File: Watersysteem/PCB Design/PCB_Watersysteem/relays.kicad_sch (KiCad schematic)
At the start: 21 parts, among them J14 Pomp1, J15 Pomp2, J16 Pomp3, J17 Pomp4, K1 AHQSS105DM2FA0G, K2 AHQSS105DM2FA0G, K3 AHQSS105DM2FA0G, K4 AHQSS105DM2FA0G, K5 AHQSS105DM2FA0G, K6 AHQSS105DM2FA0G, K7 AHQSS105DM2FA0G, Q1 PN2222A

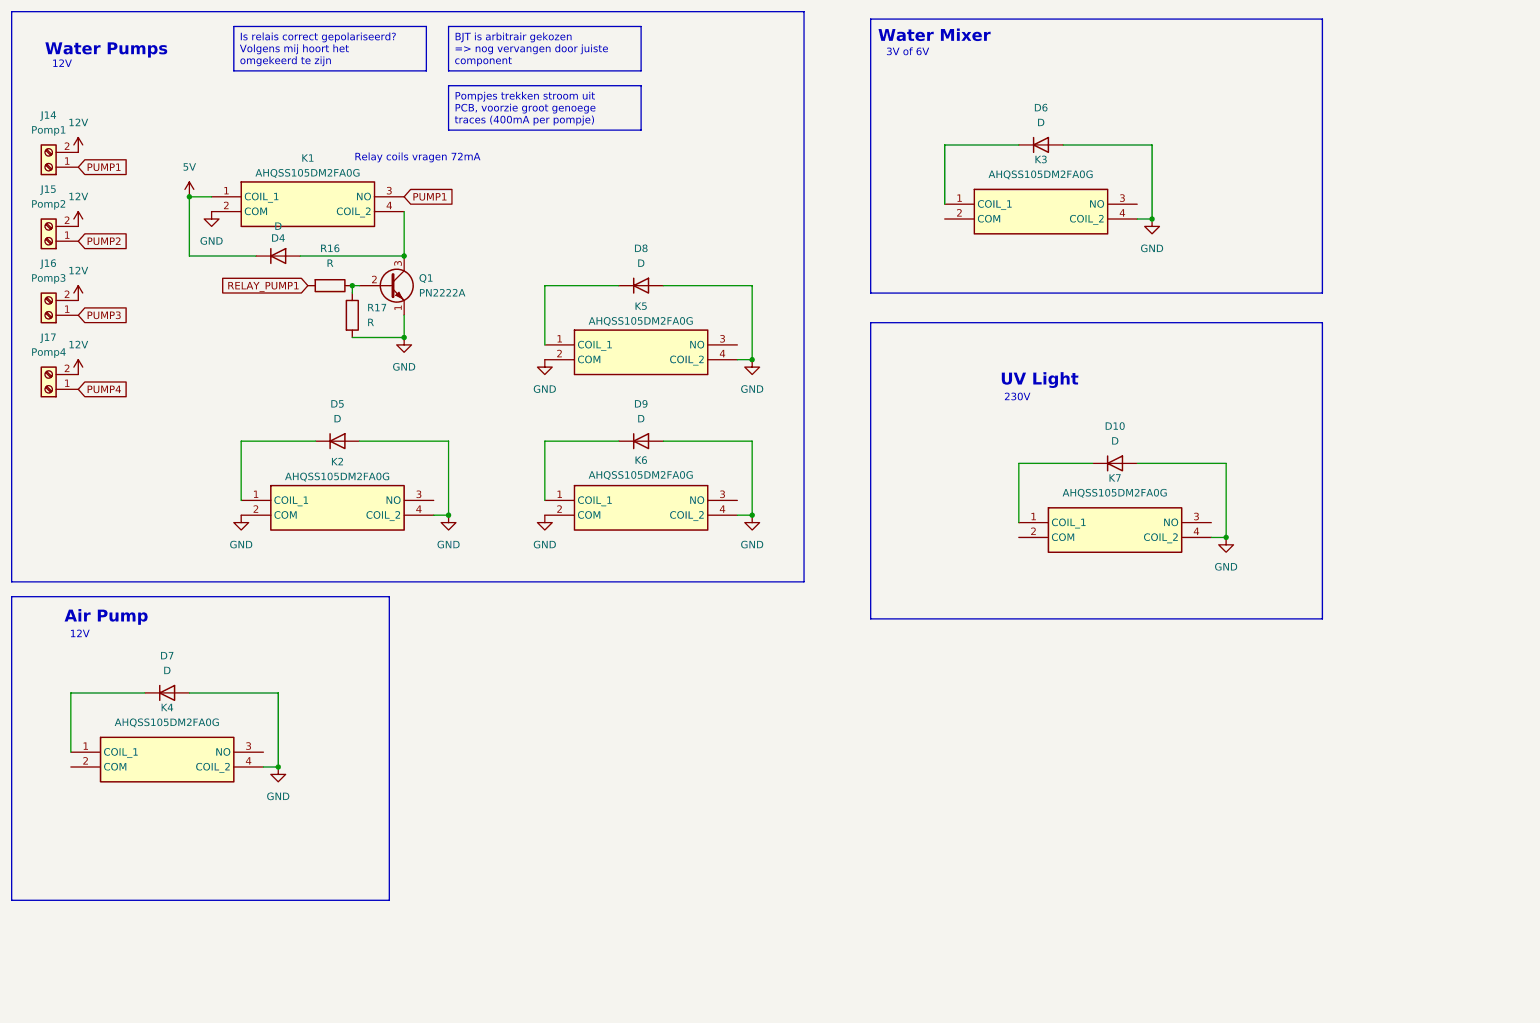
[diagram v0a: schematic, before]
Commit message: Update PCB
Extra terminals
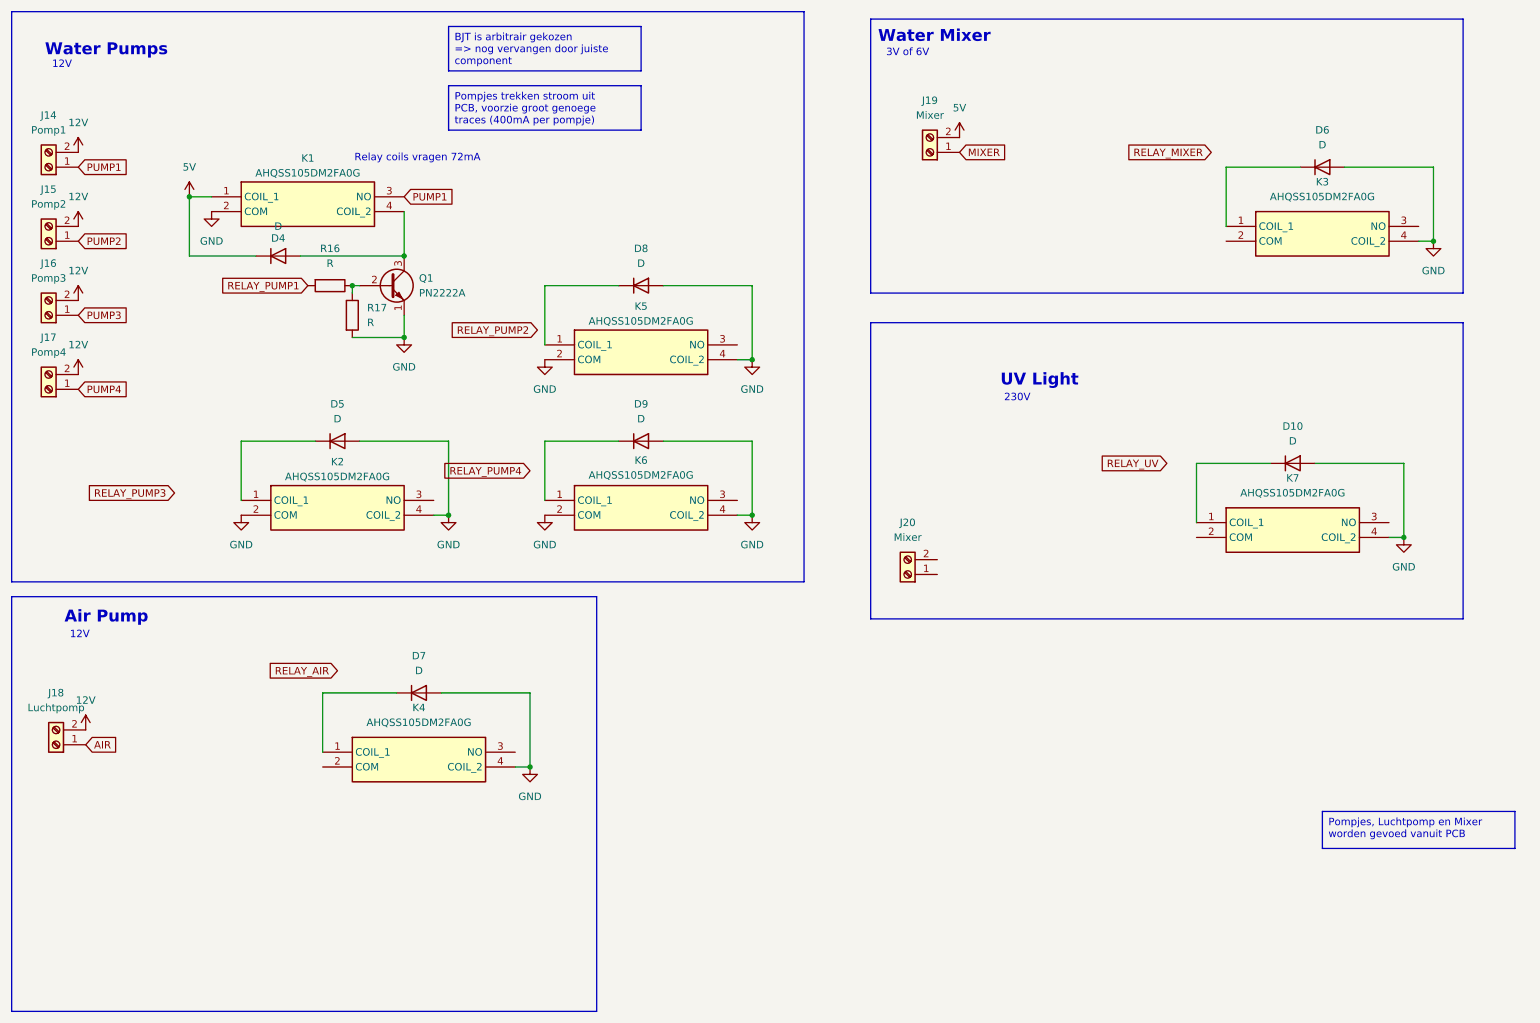
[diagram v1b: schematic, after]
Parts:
- added J18: Luchtpomp, symbol Connector:Screw_Terminal_01x02
- added J19, J20: Mixer, symbol Connector:Screw_Terminal_01x02
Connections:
- net 12V: now also J18.2 (Pin_2)
- net 5V: now also J19.2 (Pin_2)
- new net AIR: J18.1 (Pin_1)
- new net MIXER: J19.1 (Pin_1)
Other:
- moved on the sheet: D10, D6, D7, K3, K4, K7

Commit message: Update PCB
relaisschakelingen verder afgewerkt, endstops afgewerkt, bezig met ultrasone sensors
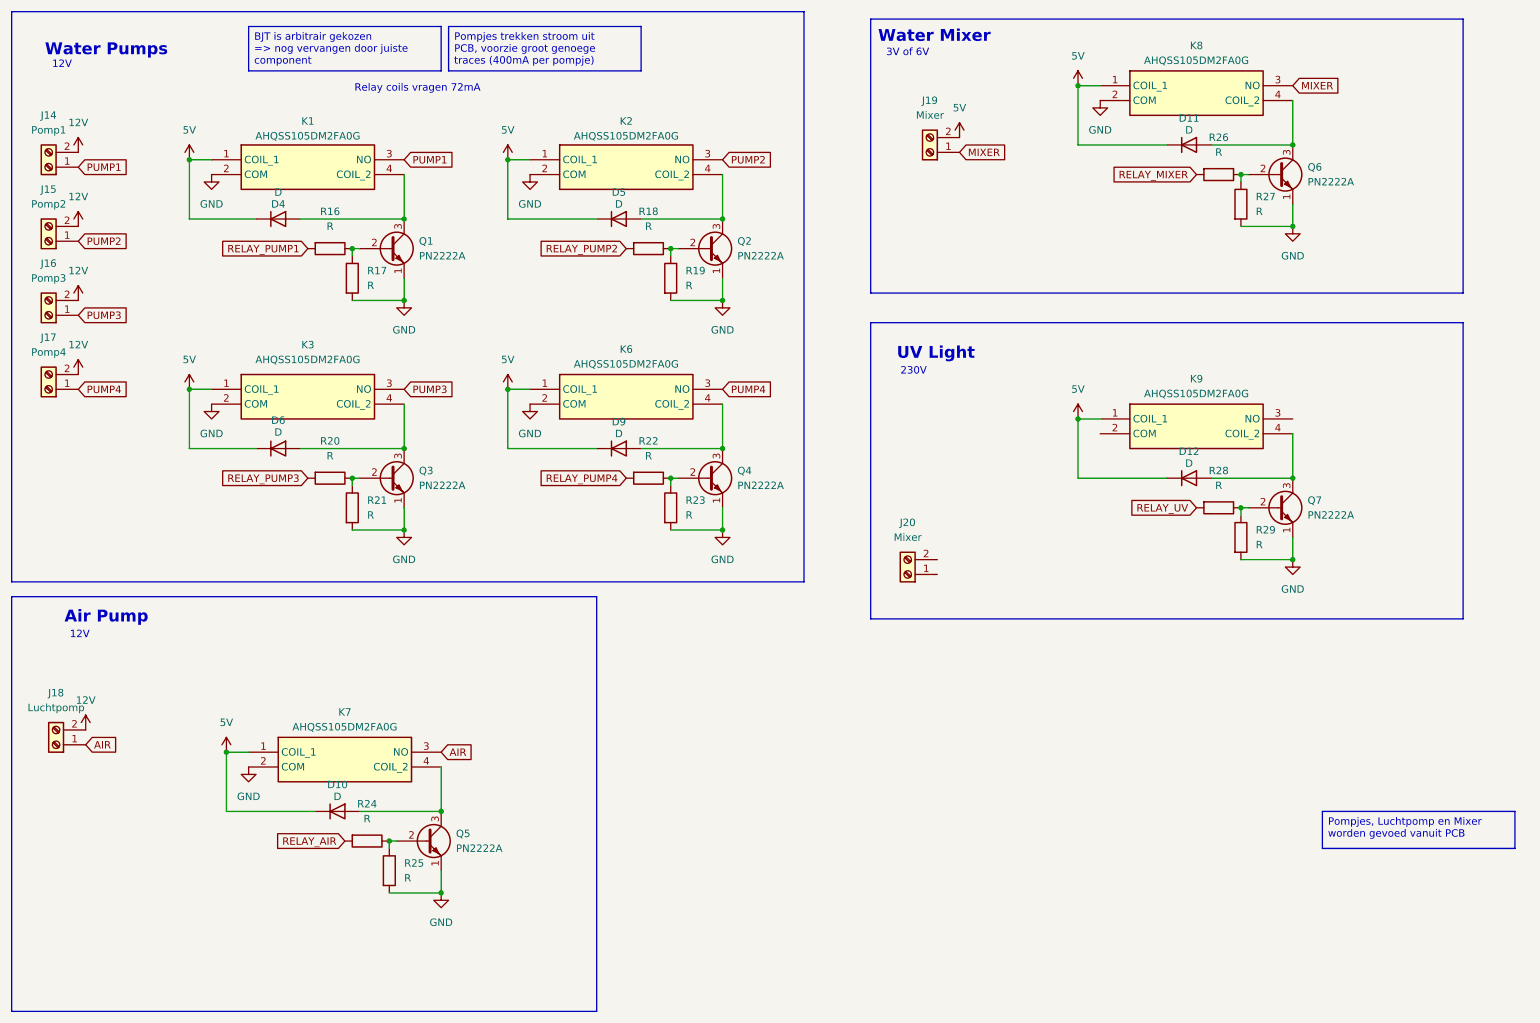
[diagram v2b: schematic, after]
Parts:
- removed D7, D8: D, symbol Device:D
- removed K4, K5: AHQSS105DM2FA0G, SamacSys_Parts:AHQSS105DM2FA0G, symbol SamacSys_Parts:AHQSS105DM2FA0G
- added D11, D12: D, symbol Device:D
- added K8, K9: AHQSS105DM2FA0G, SamacSys_Parts:AHQSS105DM2FA0G, symbol SamacSys_Parts:AHQSS105DM2FA0G
- added Q2, Q3, Q4, Q5, Q6, Q7: PN2222A, Package_TO_SOT_THT:TO-92_Inline, symbol Transistor_BJT:PN2222A
- added R18, R19, R20, R21, R22, R23, R24, R25, R26, R27, R28, R29: R, symbol Device:R
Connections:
- net 5V: now also D10.1 (K), D5.1 (K), D6.1 (K), D9.1 (K), K2.1 (COIL_1), K3.1 (COIL_1), K6.1 (COIL_1), K7.1 (COIL_1), D11.1 (K), D12.1 (K), K8.1 (COIL_1), K9.1 (COIL_1)
- net AIR: now also K7.3 (NO)
- net GND: now also K3.2 (COM), K7.2 (COM), K8.2 (COM), Q2.1 (E), Q3.1 (E), Q4.1 (E), Q5.1 (E), Q6.1 (E), Q7.1 (E), R19.2, R21.2, R23.2, R25.2, R27.2, R29.2; no longer D10.2 (A), D5.2 (A), D6.2 (A), D9.2 (A), K2.4 (COIL_2), K3.4 (COIL_2), K6.4 (COIL_2), K7.4 (COIL_2)
- net MIXER: now also K8.3 (NO)
- net PUMP2: now also K2.3 (NO)
- net PUMP3: now also K3.3 (NO)
- net PUMP4: now also K6.3 (NO)
- net RELAY_AIR: now also R24.2
- net RELAY_MIXER: now also R26.2
- net RELAY_PUMP2: now also R18.2
- net RELAY_PUMP3: now also R20.2
- net RELAY_PUMP4: now also R22.2
- net RELAY_UV: now also R28.2
- new net: Q7.2 (B), R28.1, R29.1
- new net: Q3.2 (B), R20.1, R21.1
- new net: D6.2 (A), K3.4 (COIL_2), Q3.3 (C)
- new net: D5.2 (A), K2.4 (COIL_2), Q2.3 (C)
- new net: Q2.2 (B), R18.1, R19.1
- new net: Q4.2 (B), R22.1, R23.1
- new net: D11.2 (A), K8.4 (COIL_2), Q6.3 (C)
- new net: D12.2 (A), K9.4 (COIL_2), Q7.3 (C)
- new net: D10.2 (A), K7.4 (COIL_2), Q5.3 (C)
- new net: Q6.2 (B), R26.1, R27.1
- new net: Q5.2 (B), R24.1, R25.1
- new net: D9.2 (A), K6.4 (COIL_2), Q4.3 (C)
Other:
- moved on the sheet: D4, D5, D6, D9, K1, K2, K3, K6, Q1, R16, R17

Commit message: Update PCB
deel footprints geselecteerd, hoogtesensoren ingesteld
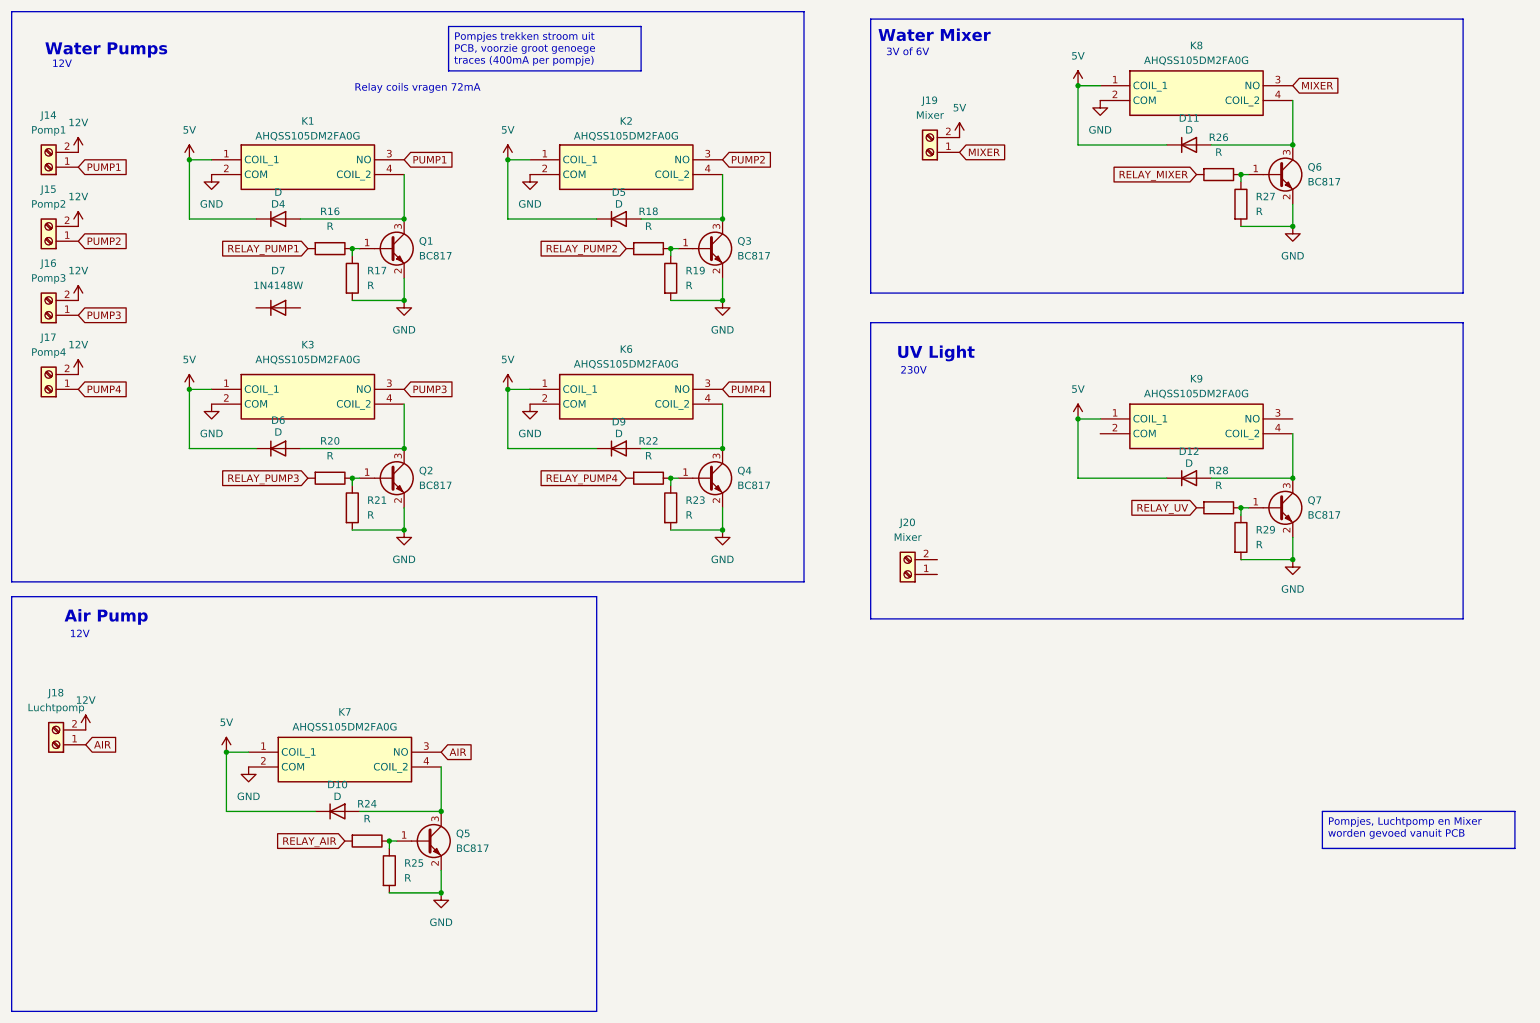
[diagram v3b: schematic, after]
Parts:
- removed Q1, Q2, Q3, Q4, Q5, Q6, Q7: PN2222A, Package_TO_SOT_THT:TO-92_Inline, symbol Transistor_BJT:PN2222A
- added D7: 1N4148W, Diode_SMD:D_SOD-123, symbol Diode:1N4148W
- added Q1, Q2, Q3, Q4, Q5, Q6, Q7: BC817, Package_TO_SOT_SMD:SOT-23, symbol Transistor_BJT:BC817
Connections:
- net GND: now also Q1.2 (E), Q2.2 (E), Q3.2 (E), Q4.2 (E), Q5.2 (E), Q6.2 (E), Q7.2 (E)
- net at R16.1, R17.1: now also Q1.1 (B)
- net at R28.1, R29.1: now also Q7.1 (B)
- net at R20.1, R21.1: now also Q2.1 (B)
- net at D6.2 (A), K3.4 (COIL_2): now also Q2.3 (C)
- net at D5.2 (A), K2.4 (COIL_2): now also Q3.3 (C)
- net at R18.1, R19.1: now also Q3.1 (B)
- net at R22.1, R23.1: now also Q4.1 (B)
- net at D4.2 (A), K1.4 (COIL_2): now also Q1.3 (C)
- net at D11.2 (A), K8.4 (COIL_2): now also Q6.3 (C)
- net at D12.2 (A), K9.4 (COIL_2): now also Q7.3 (C)
- net at D10.2 (A), K7.4 (COIL_2): now also Q5.3 (C)
- net at R26.1, R27.1: now also Q6.1 (B)
- net at R24.1, R25.1: now also Q5.1 (B)
- net at D9.2 (A), K6.4 (COIL_2): now also Q4.3 (C)

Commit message: PCB update
Testpunten, relaisschakelingen afgewerkt, adres io expander wijzigbaar, enkele footprints
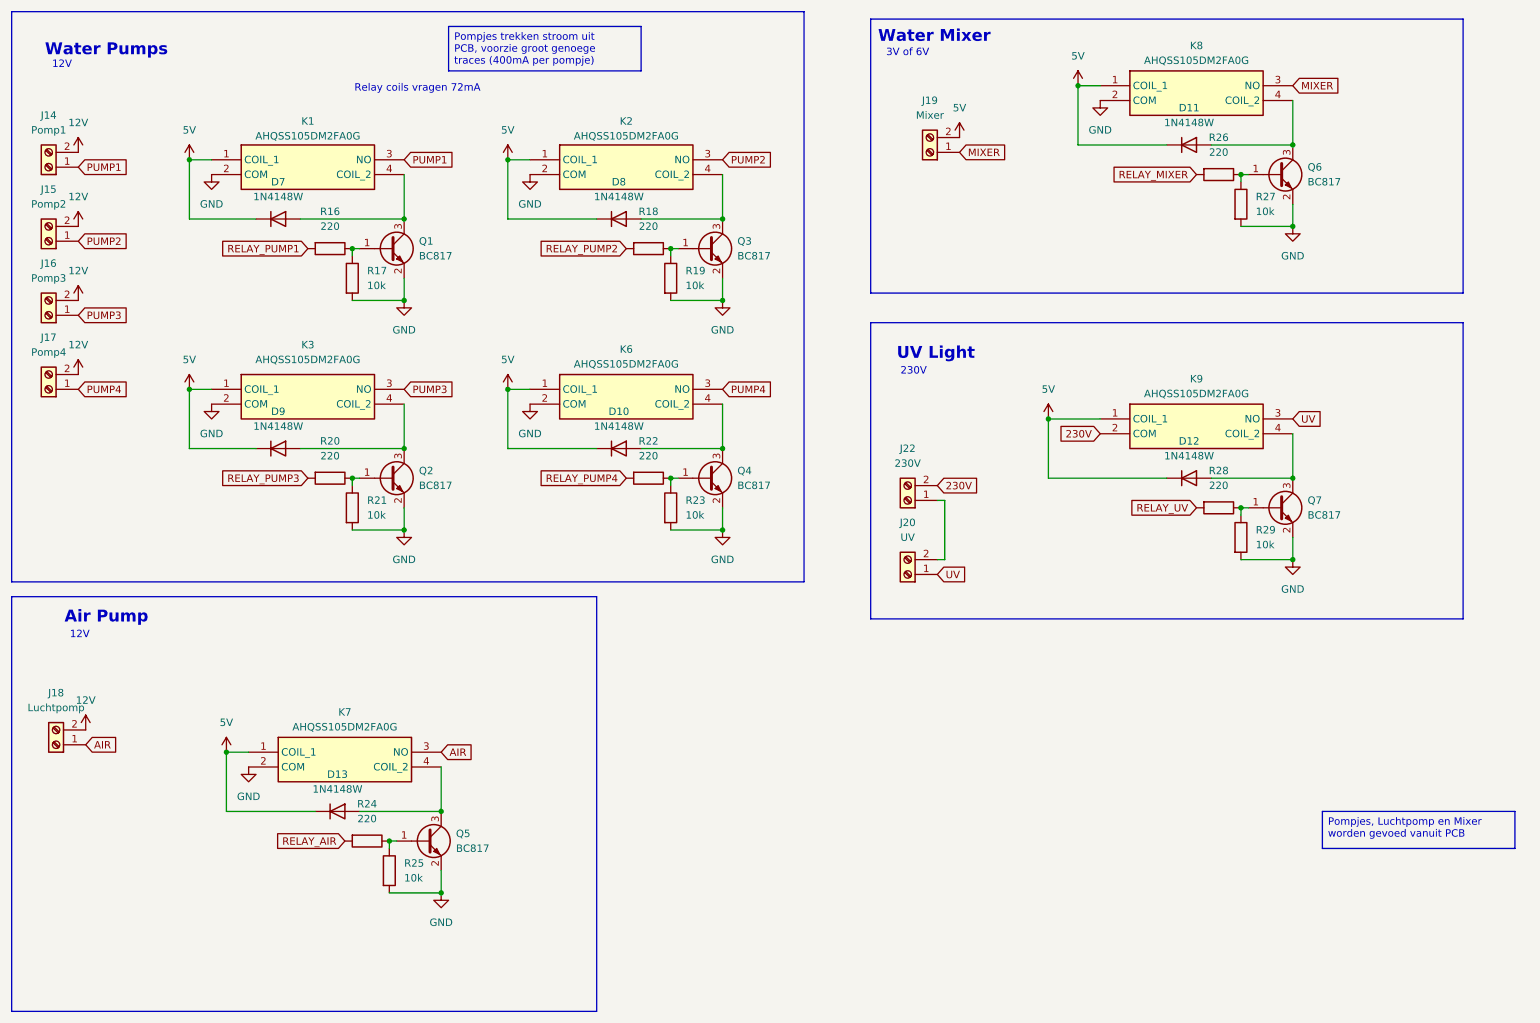
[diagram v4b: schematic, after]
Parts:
- removed D10, D11, D12, D4, D5, D6, D9: D, symbol Device:D
- added D10, D11, D12, D13, D8, D9: 1N4148W, Diode_SMD:D_SOD-123, symbol Diode:1N4148W
- added J22: 230V, symbol Connector:Screw_Terminal_01x02
- J20: value Mixer -> UV
- R16, R18, R20, R22, R24, R26, R28: value R -> 220; footprint (none) -> Resistor_SMD:R_0805_2012Metric_Pad1.20x1.40mm_HandSolder
- R17, R19, R21, R23, R25, R27, R29: value R -> 10k; footprint (none) -> Resistor_SMD:R_0805_2012Metric_Pad1.20x1.40mm_HandSolder
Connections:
- net 5V: now also D7.1 (K), D10.1 (K), D11.1 (K), D12.1 (K), D13.1 (K), D8.1 (K), D9.1 (K)
- net at K2.4 (COIL_2), Q3.3 (C): now also D8.2 (A)
- net at K8.4 (COIL_2), Q6.3 (C): now also D11.2 (A)
- net at K7.4 (COIL_2), Q5.3 (C): now also D13.2 (A)
- net at K1.4 (COIL_2), Q1.3 (C): now also D7.2 (A)
- net UV: now reaches J20.1 (Pin_1)
- net UV: now also K9.3 (NO)
- net at J20.2 (Pin_2): now also J22.1 (Pin_1)
- net 230V: now reaches K9.2 (COM)
- net 230V: now also J22.2 (Pin_2)
- net at K9.4 (COIL_2), Q7.3 (C): now also D12.2 (A)
- net at K3.4 (COIL_2), Q2.3 (C): now also D9.2 (A)
- net at K6.4 (COIL_2), Q4.3 (C): now also D10.2 (A)
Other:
- moved on the sheet: D7
